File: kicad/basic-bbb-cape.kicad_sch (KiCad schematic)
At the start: 7 parts, among them J8 BBB_P8, J9 BBB_P9, U1 CAT24C32YI-GT3

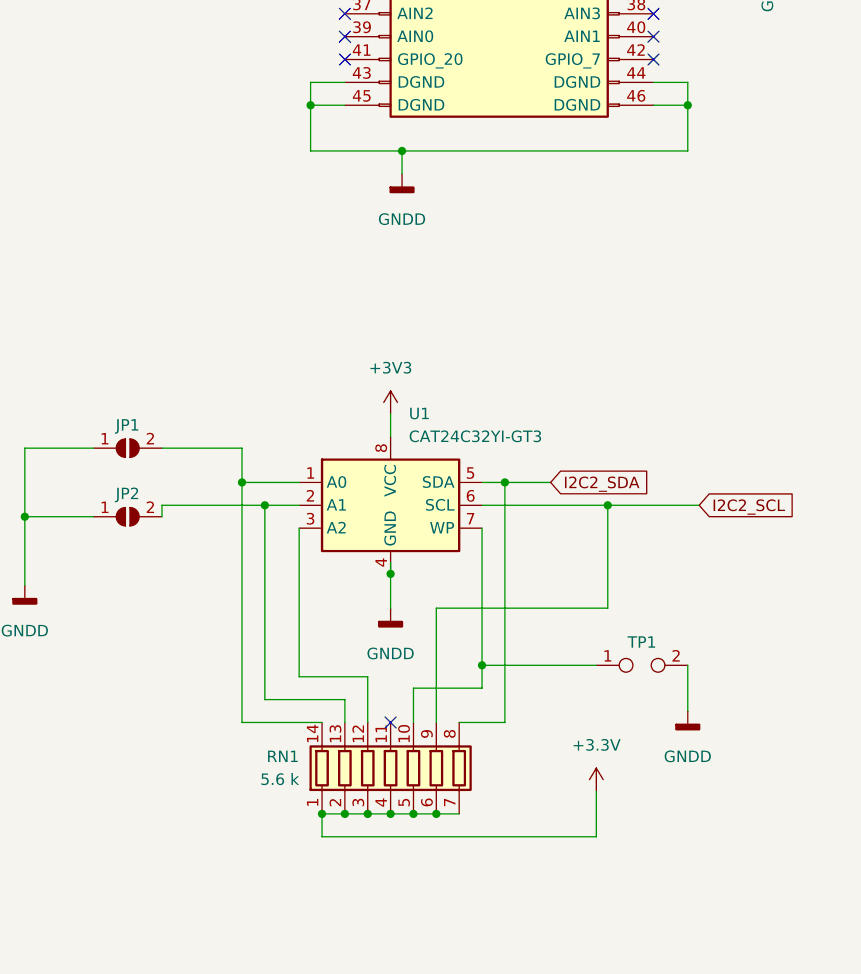
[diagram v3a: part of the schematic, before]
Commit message: Rotate RP1 and U1 180 degrees
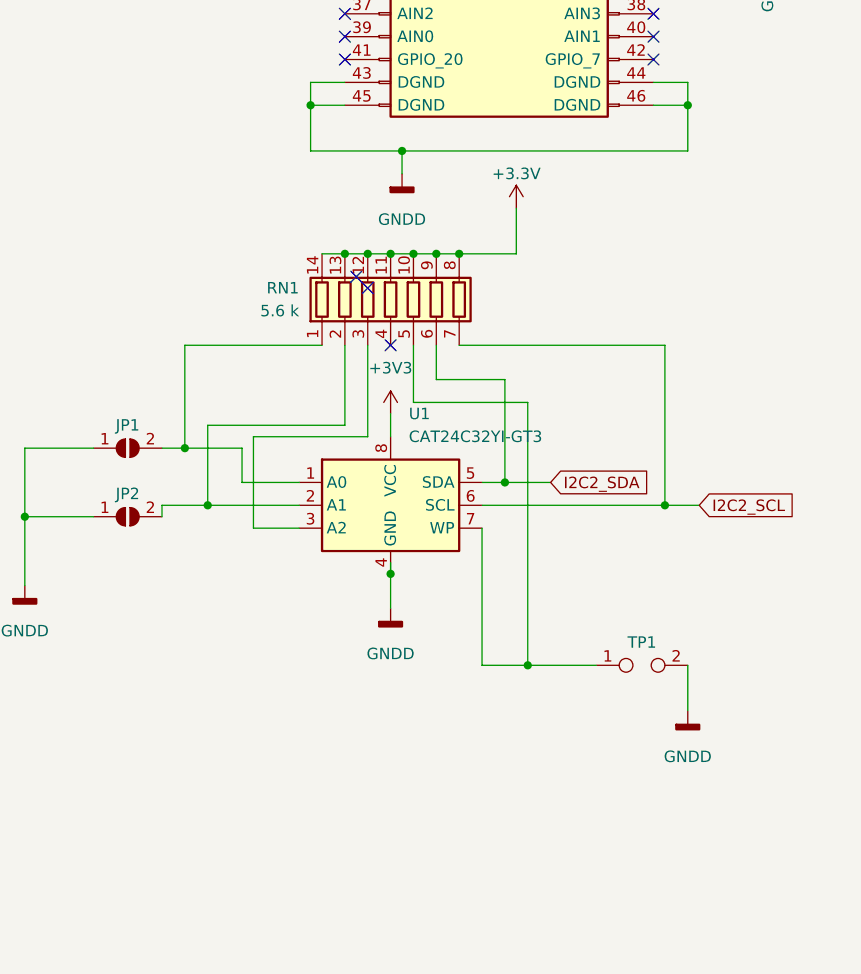
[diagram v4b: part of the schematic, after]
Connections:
- net +3V3: now also RN1.10 (R5.2), RN1.11 (R4.2), RN1.12 (R3.2), RN1.13 (R2.2), RN1.14 (R1.2), RN1.8 (R7.2), RN1.9 (R6.2); no longer RN1.1 (R1.1), RN1.2 (R2.1), RN1.3 (R3.1), RN1.4 (R4.1), RN1.5 (R5.1), RN1.6 (R6.1), RN1.7 (R7.1)
- net I2C2_SCL: now also RN1.7 (R7.1); no longer RN1.9 (R6.2)
- net I2C2_SDA: now also RN1.6 (R6.1); no longer RN1.8 (R7.2)
- net at JP1.2 (B), U1.1 (A0): now also RN1.1 (R1.1); no longer RN1.14 (R1.2)
- net at JP2.2 (B), U1.2 (A1): now also RN1.2 (R2.1); no longer RN1.13 (R2.2)
- net at U1.3 (A2): now also RN1.3 (R3.1); no longer RN1.12 (R3.2)
- net at TP1.1, U1.7 (WP): now also RN1.5 (R5.1); no longer RN1.10 (R5.2)
- no-connect marks 75 -> 77
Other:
- moved on the sheet: RN1

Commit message: Add solder jumper to PCB
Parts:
- JP1, JP2: footprint (none) -> Jumper:SolderJumper-2_P1.3mm_Open_TrianglePad1.0x1.5mm
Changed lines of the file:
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@@
       (effects (font (size 1.27 1.27)) hide)
     )
-    (property "Footprint" "" (id 2) (at 31.75 130.81 0)
+    (property "Footprint" "Jumper:SolderJumper-2_P1.3mm_Open_TrianglePad1.0x1.5mm" (id 2) (at 31.75 130.81 0)
       (effects (font (size 1.27 1.27)) hide)
     )
@@
     (pin "2")
   )
-  (symbol (lib_id "Jumper:SolderJumper_2_Open") (at 31.75 123.19 0) (unit 1)
+  (symbol (lib_name "SolderJumper_2_Open_1") (lib_id "Jumper:SolderJumper_2_Open") (at 31.75 123.19 0) (unit 1)
     (in_bom yes) (on_board yes)
     (property "Reference" "JP1" (id 0) (at 31.75 120.65 0))
@@
       (effects (font (size 1.27 1.27)) hide)
     )
-    (property "Footprint" "" (id 2) (at 31.75 123.19 0)
+    (property "Footprint" "Jumper:SolderJumper-2_P1.3mm_Open_TrianglePad1.0x1.5mm" (id 2) (at 31.75 123.19 0)
       (effects (font (size 1.27 1.27)) hide)
     )
@@
     )
     (path "/fe024c77-8b5d-48f2-aac3-fec332431e02"
-      (reference "JP1") (unit 1) (value "SolderJumper_2_Open") (footprint "")
+      (reference "JP1") (unit 1) (value "SolderJumper_2_Open") (footprint "Jumper:SolderJumper-2_P1.3mm_Open_TrianglePad1.0x1.5mm")
     )
     (path "/311e7bbb-a30b-483f-9c86-e38e5c8c6715"
-      (reference "JP2") (unit 1) (value "SolderJumper_2_Open") (footprint "")
+      (reference "JP2") (unit 1) (value "SolderJumper_2_Open") (footprint "Jumper:SolderJumper-2_P1.3mm_Open_TrianglePad1.0x1.5mm")
     )
     (path "/5a7dfcd7-0335-4ce5-94ea-54b61d3b55cb"

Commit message: Update schematic and PCB
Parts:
- removed RN1: 5.6 k, Package_DIP:DIP-14_W7.62mm_Socket_LongPads, symbol Device:R_Pack07
- added RN1: R_Pack07, Package_DIP:DIP-14_W7.62mm_Socket_LongPads, symbol r_pack_eeprom:R_Pack07
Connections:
- net +3V3: now also RN1.1 (R1.1), RN1.2 (R2.1), RN1.3 (R3.1), RN1.4 (R4.1), RN1.5 (R5.1), RN1.6 (R6.1), RN1.7 (R7.1)
- net I2C2_SCL: now also RN1.8 (R7.2)
- net I2C2_SDA: now also RN1.9 (R6.2)
- net at JP1.2 (B), U1.1 (A0): now also RN1.13 (R2.2)
- net at JP2.2 (B), U1.2 (A1): now also RN1.12 (R3.2)
- net at U1.3 (A2): now also RN1.11 (R4.2)
- net at TP1.1, U1.7 (WP): now also RN1.10 (R5.2)
- no-connect marks 77 -> 75
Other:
- moved on the sheet: JP1, JP2, TP1, U1

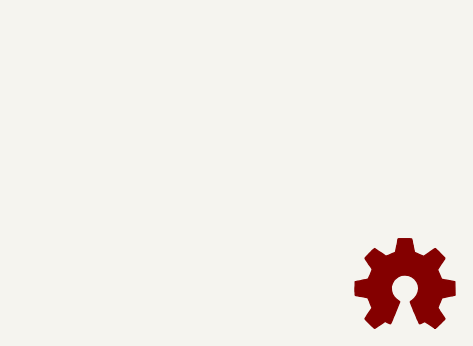
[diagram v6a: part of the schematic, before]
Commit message: Resize schematic to 8x11 inch and reset PCH closer to defaults
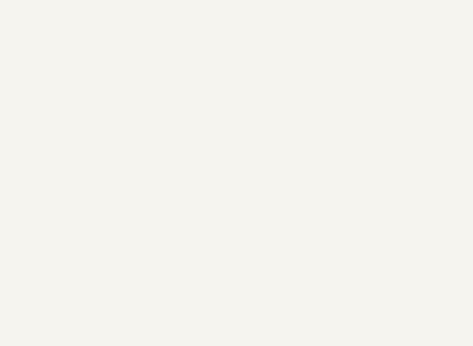
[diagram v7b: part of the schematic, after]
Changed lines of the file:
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@@
 (kicad_sch (version 20211123) (generator eeschema)
-  (paper "A4")
+  (paper "USLetter")
   (title_block
     (comment 2 "CC BY 4.0")
@@
     (stroke (width 0) (type default) (color 0 0 0 0))
   )
-  (image (at 265.43 173.99) (scale 2)
-    (data
-      iVBORw0KGgoAAAANSUhEUgAAAEAAAABACAYAAACqaXHeAAAABHNCSVQICAgIfAhkiAAAA8JJREFU
-      eJzt2k1oXFUYxvHfNM197zSJhdb6gR9VrNaKpS4UXLipIqigCwXBTXVRRBTE0qIbN+6UIkhXoviB
-      qIguBCviomqVLkVLISIK2io2rZZWtJWmrRkXkys3Y2oyM3fubcj9w5B5z8k575PnnvPOmXtDTU1N
-      Tc3ipfF/nUGrLCHzZXIOzYVyrhkwCD1Lip5woVEbULWAqlnay6CyakMZBa8nAxi8uLJMXvRboDag
-      agFVUxtQtYCqqQ2oWkDV1AaUlCdKytM1ZRkwWVKerqm3QNUCqqY2oGoBVVMbULWAqln0BvR8R+hc
-      u2XeKz0ZUOrDiQHT8woYJLOtrkGZXmgNCL5NuD4Xfx7cnotfCrZlccptwfdY1jnXJI3sVaTGruh2
-      nwd/YSSLE46MckGu/7sOg3amPJjlmu2V11F63eky4dLgTC5uBH/LXcHglNw3w+DYKKuyXAvdgKEO
-      A5ZMG3C2uHG2+Tvb5zCgry1SZA3oFNLqaJ/SNiBy/b9nK2A25nkB+loVRRpwRnuJZzWg1cot8Wn2
-      J1ydi/ec4a4CNXRN0SfBnxKuzIIG46fZkOvf3eCOXP8LLZ42y6cA5Zw3CjWgwddLuDGLW3yKO3PJ
-      XsMjps8fJ/mkxZ6UV3T8sZ2FsBK6TZ6yOeWd3Pi1wYSZlf/jYEtuWDPYHXwwwoVF6umbbhOOcX5w
-      DMtzc3wYPJqLrwoOD8/cGpHyTPBbsCPhgYT1GJn+2ZOevuklYcrbwdYsHmZDMDHGyqwt4f7gxyaX
-      5Mc2uSzhyZQ3g33B8WBfP3r6opeECeuDgxjLzbM9eK9j7m3B/mFuGqSevug1YcKrwfb8VClfdux9
-      CfcFE8GLnauhSD0902vCUVYFB5vcnLU1uTz4OeHe/O+OsTLl2YQjwa7g+ZRN0zViNF8rFowB02Pv
-      CX7AiqxtmBuCQ8FjswxZnnJrsCXh9WBv8Gewtwg9PdFvwuC5YBeGc21rgq+Cj4I1ZerpmgISDgXv
-      J7xh5qErCbYGvwYvp6wuSc9/mPN/hQs4jjaDnfhjkk04nnWMsfI0j7d4Ar9gvMH4FOP45lT7u8MV
-      p9pxUXpmUIYBEMEObGzw8El2d/SPDrN2iHVY1+Ja7fercWCS6wrWM0/VBS+54O5gf8q7wTVV66kq
-      4bKEp4LDKW81ucU8r+pCrQFn47xgMx7CqgaftfgCB6Y4lDBxgqMjrDjBoUHpqdKAf0nb9xA2ttoH
-      p0txES7WPkMcnWy/X/g1oF8GoWfRPxusDahaQNXUBlQtoGrmfDp8rn0S1BTMP+iE3ieWJjVeAAAA
-      AElFTkSuQmCC
-    )
-  )
   (global_label "I2C2_SCL" (shape input) (at 38.1 52.07 180) (fields_autoplaced)
     (effects (font (size 1.27 1.27)) (justify right))
@@
     )
     (pin "1")
-  )
-  (symbol (lib_id "Graphic:Logo_Open_Hardware_Small") (at 275.59 175.26 0) (unit 1)
-    (in_bom yes) (on_board yes)
-    (property "Reference" "#LOGO1" (id 0) (at 275.59 168.275 0)
-      (effects (font (size 1.27 1.27)) hide)
-    )
-    (property "Value" "Logo_Open_Hardware_Small" (id 1) (at 275.59 180.975 0)
-      (effects (font (size 1.27 1.27)) hide)
-    )
-    (property "Footprint" "" (id 2) (at 275.59 175.26 0)
-      (effects (font (size 1.27 1.27)) hide)
-    )
-    (property "Datasheet" "~" (id 3) (at 275.59 175.26 0)
-      (effects (font (size 1.27 1.27)) hide)
-    )
   )
   (symbol (lib_id "power:+3.3V") (at 60.96 101.6 0) (unit 1)
@@
   )
   (symbol_instances
-    (path "/00000000-0000-0000-0000-00005cd22ef9"
-      (reference "#LOGO1") (unit 1) (value "Logo_Open_Hardware_Small") (footprint "")
-    )
     (path "/00000000-0000-0000-0000-0000558985d8"
       (reference "#PWR0101") (unit 1) (value "VDD_ADC") (footprint "")
